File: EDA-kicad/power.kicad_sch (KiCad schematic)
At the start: 93 parts, among them SW1 EG25-switch-CSS-1210MC, SW2 MIC-switch-CSS-1210MC, SW3 CAM-switch-CSS-1210MC, U10 22V-boost-AP3032KTR-G1, U11 MP3429GL-Z, U7 BQ25792RQMR, U8 TPS65023BRSBR, U9 BAT-CONNECTOR-FLTS22WR00

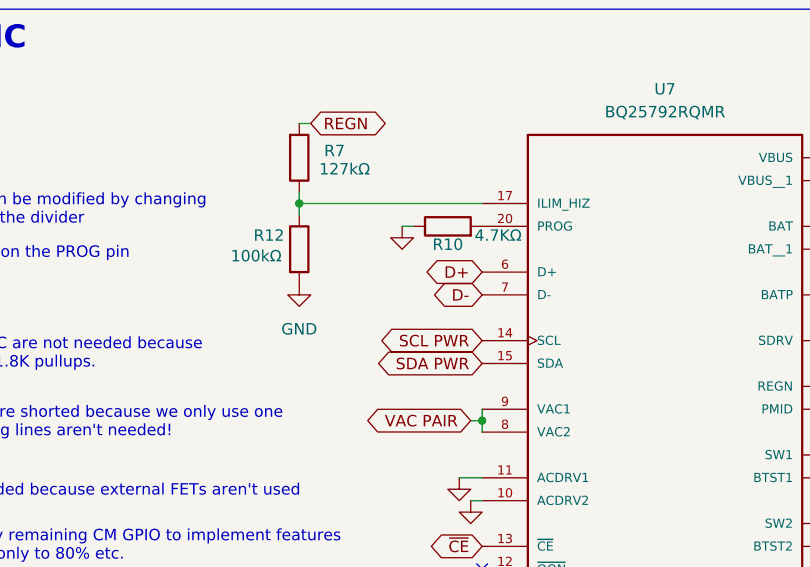
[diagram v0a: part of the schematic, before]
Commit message: connect charger to usb switch
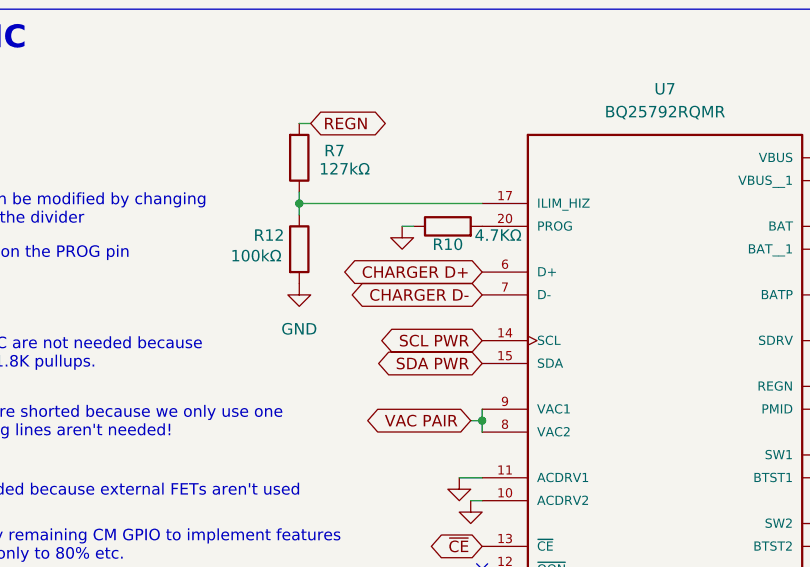
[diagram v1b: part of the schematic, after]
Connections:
- net D+ renamed CHARGER D+
- net D- renamed CHARGER D-
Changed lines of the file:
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@@
+		)
+	)
+	(global_label "CHARGER D+"
+		(shape bidirectional)
+		(at 90.17 80.01 180)
+		(fields_autoplaced yes)
+		(effects
+			(font
+				(size 1.27 1.27)
+			)
+			(justify right)
+		)
+		(property "Intersheetrefs" "${INTERSHEET_REFS}"
+			(at 73.6154 80.01 0)
+			(effects
+				(font
+					(size 1.27 1.27)
+				)
+				(justify right)
+				(hide yes)
+			)
 		)
 	)
@@
 		)
 	)
-	(global_label "D-"
+	(global_label "EN3V3A SW OUT"
+		(shape bidirectional)
+		(at 110.49 185.42 0)
+		(fields_autoplaced yes)
+		(effects
+			(font
+				(size 1.27 1.27)
+			)
+			(justify left)
+		)
+		(property "Intersheetrefs" "${INTERSHEET_REFS}"
+			(at 129.8869 185.42 0)
+			(effects
+				(font
+					(size 1.27 1.27)
+				)
+				(justify left)
+				(hide yes)
+			)
+		)
+	)
+	(global_label "USBC POW"
+		(shape bidirectional)
+		(at 135.89 67.31 0)
+		(fields_autoplaced yes)
+		(effects
+			(font
+				(size 1.27 1.27)
+			)
+			(justify left)
+		)
+		(property "Intersheetrefs" "${INTERSHEET_REFS}"
+			(at 148.4026 67.2306 0)
+			(effects
+				(font
+					(size 1.27 1.27)
+				)
+				(justify left)
+				(hide yes)
+			)
+		)
+	)
+	(global_label "SYS"
+		(shape bidirectional)
+		(at 49.53 227.33 180)
+		(fields_autoplaced yes)
+		(effects
+			(font
+				(size 1.27 1.27)
+			)
+			(justify right)
+		)
+		(property "Intersheetrefs" "${INTERSHEET_REFS}"
+			(at 41.9259 227.33 0)
+			(effects
+				(font
+					(size 1.27 1.27)
+				)
+				(justify right)
+				(hide yes)
+			)
+		)
+	)
+	(global_label "CHARGER D-"
 		(shape bidirectional)
 		(at 90.17 82.55 180)
@@
 		)
 		(property "Intersheetrefs" "${INTERSHEET_REFS}"
-			(at 83.2311 82.55 0)
-			(effects
-				(font
-					(size 1.27 1.27)
-				)
-				(justify right)
-				(hide yes)
-			)
-		)
-	)
-	(global_label "EN3V3A SW OUT"
-		(shape bidirectional)
-		(at 110.49 185.42 0)
-		(fields_autoplaced yes)
-		(effects
-			(font
-				(size 1.27 1.27)
-			)
-			(justify left)
-		)
-		(property "Intersheetrefs" "${INTERSHEET_REFS}"
-			(at 129.8869 185.42 0)
-			(effects
-				(font
-					(size 1.27 1.27)
-				)
-				(justify left)
-				(hide yes)
-			)
-		)
-	)
-	(global_label "D+"
-		(shape bidirectional)
-		(at 90.17 80.01 180)
-		(fields_autoplaced yes)
-		(effects
-			(font
-				(size 1.27 1.27)
-			)
-			(justify right)
-		)
-		(property "Intersheetrefs" "${INTERSHEET_REFS}"
-			(at 83.2311 80.01 0)
-			(effects
-				(font
-					(size 1.27 1.27)
-				)
-				(justify right)
-				(hide yes)
-			)
-		)
-	)
-	(global_label "USBC POW"
-		(shape bidirectional)
-		(at 135.89 67.31 0)
-		(fields_autoplaced yes)
-		(effects
-			(font
-				(size 1.27 1.27)
-			)
-			(justify left)
-		)
-		(property "Intersheetrefs" "${INTERSHEET_REFS}"
-			(at 148.4026 67.2306 0)
-			(effects
-				(font
-					(size 1.27 1.27)
-				)
-				(justify left)
-				(hide yes)
-			)
-		)
-	)
-	(global_label "SYS"
-		(shape bidirectional)
-		(at 49.53 227.33 180)
-		(fields_autoplaced yes)
-		(effects
-			(font
-				(size 1.27 1.27)
-			)
-			(justify right)
-		)
-		(property "Intersheetrefs" "${INTERSHEET_REFS}"
-			(at 41.9259 227.33 0)
-			(effects
-				(font
+			(at 73.6154 82.55 0)
+			(effects
+				(font
